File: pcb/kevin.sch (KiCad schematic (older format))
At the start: 70 parts, among them J1 battery, J2 joystick, J3 eink, J3-DRV1 eink, SW00 SW_Push, SW01 SW_Push, SW02 SW_Push, SW03 SW_Push, SW04 SW_Push, SW05 SW_Push, SW10 SW_Push, SW11 SW_Push, SW12 SW_Push, SW13 SW_Push, SW14 SW_Push, SW15 SW_Push, SW20 SW_Push, SW21 SW_Push, SW22 SW_Push, SW23 SW_Push, SW24 SW_Push, SW25 SW_Push, SW32 SW_Push, SW33 SW_Push, SW34 SW_Push, SW35 SW_Push, U1 nice_nano

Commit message: Prepare reversible matrix (kailth pg1350 and diode footprints) Routing e-ink reset to mcu Keys placement
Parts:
- D00, D01, D02, D03, D04, D05, D10, D11, D12, D13, D14, D15, D20, D21, D22, D23, D24, D25, D32, D33, D34, D35, D_EI1: footprint Diode_SMD:D_SOD-123 -> kevin:D_SOD-123_reversible
- SW00, SW01, SW02, SW03, SW04, SW05, SW10, SW11, SW12, SW13, SW14, SW15, SW20, SW21, SW22, SW23, SW24, SW25, SW32, SW33, SW34, SW35: footprint Keebio-Parts:Kailh-PG1350-1u-reversible -> kevin:Kailh-PG1350-1u-choc-reversible
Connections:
- net labels added: eink_reset
- no-connect marks 5 -> 4

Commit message: General cleaning
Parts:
- D_EI1: footprint kevin:D_SOD-123_reversible -> Diode_SMD:D_SOD-123
- U1: footprint nice-nano-kicad:nice_nano -> kevin:nice_nano_v2_reversible; symbol nice_nano:nice_nano -> kevin:nice_nano_v2
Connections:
- no-connect marks 4 -> 6
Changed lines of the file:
@@
 Text GLabel 9000 2850 0    50   Input ~ 0
 row0
-Connection ~ 9000 2250
 Wire Wire Line
 	9000 2350 9000 2250
@@
 $EndComp
 $Comp
-L nice_nano:nice_nano U1
+L kevin:nice_nano_v2 U1
 U 1 1 60FB3122
 P 9700 2600
 F 0 "U1" H 9700 3537 60  0000 C CNN
 F 1 "nice_nano" H 9700 3431 60  0000 C CNN
-F 2 "nice-nano-kicad:nice_nano" V 10750 100 60  0001 C CNN
+F 2 "kevin:nice_nano_v2_reversible" V 10750 100 60  0001 C CNN
 F 3 "" V 10750 100 60  0001 C CNN
 	1    9700 2600
@@
 F 0 "D_EI1" V 3496 5920 50  0000 R CNN
 F 1 "MBR0530" V 3405 5920 50  0000 R CNN
-F 2 "kevin:D_SOD-123_reversible" H 3450 6000 50  0001 C CNN
+F 2 "Diode_SMD:D_SOD-123" H 3450 6000 50  0001 C CNN
 F 3 "~" H 3450 6000 50  0001 C CNN
 	1    3450 6000
@@
 Text GLabel 9000 2050 0    50   Input ~ 0
 eink_reset
+NoConn ~ 10400 1950
+NoConn ~ 9000 1950
 $EndSCHEMATC

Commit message: prepare schema for review
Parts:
- added C20: 100nF, Capacitor_SMD:C_0805_2012Metric_Pad1.18x1.45mm_HandSolder, symbol Device:C_Small
- added C21: 4.7uF, Capacitor_SMD:C_0805_2012Metric_Pad1.18x1.45mm_HandSolder, symbol Device:C_Small
- added D40, D41, D42, D43, D44: D, kevin:D_SOD-123_reversible, symbol Device:D
- added J4: to-trackball-side, Connector_PinSocket_2.54mm:PinSocket_1x08_P2.54mm_Horizontal, symbol Connector_Generic:Conn_01x08
- added J5: trackball-side, Connector_PinSocket_2.54mm:PinSocket_1x08_P2.54mm_Horizontal, symbol Connector_Generic:Conn_01x08
- added R002, R01, R02: 10k, kevin:R_1206_reversible, symbol Device:R
- added R23: 10k, Resistor_SMD:R_1206_3216Metric_Pad1.30x1.75mm_HandSolder, symbol Device:R
- added SW_4dir1: SW_4dir-push, symbol kevin:SW_SKRH-4dir-push
- added U2: XC6206P202MR-G, Package_TO_SOT_SMD:SOT-23, symbol Regulator_Linear:XC6206PxxxMR
- added U3: PMW3360DM-T2QU, kevin:IC_PMW3360DM-T2QU, symbol kevin:PMW3360DM-T2QU
- C01: renamed from C1; footprint Capacitor_SMD:C_0805_2012Metric_Pad1.18x1.45mm_HandSolder -> kevin:C_0805_reversible
- C02: renamed from C2; footprint Capacitor_SMD:C_0805_2012Metric_Pad1.18x1.45mm_HandSolder -> kevin:C_0805_reversible
- C03: renamed from C3; footprint Capacitor_SMD:C_0805_2012Metric_Pad1.18x1.45mm_HandSolder -> kevin:C_0805_reversible
- C04: renamed from C4; footprint Capacitor_SMD:C_0805_2012Metric_Pad1.18x1.45mm_HandSolder -> kevin:C_0805_reversible
- C05: renamed from C5; footprint Capacitor_SMD:C_0805_2012Metric_Pad1.18x1.45mm_HandSolder -> kevin:C_0805_reversible
- C06: renamed from C6; footprint Capacitor_SMD:C_0805_2012Metric_Pad1.18x1.45mm_HandSolder -> kevin:C_0805_reversible
- C07: renamed from C7; footprint Capacitor_SMD:C_0805_2012Metric_Pad1.18x1.45mm_HandSolder -> kevin:C_0805_reversible
- C08: renamed from C8; footprint Capacitor_SMD:C_0805_2012Metric_Pad1.18x1.45mm_HandSolder -> kevin:C_0805_reversible
- C09: renamed from C9; footprint Capacitor_SMD:C_0805_2012Metric_Pad1.18x1.45mm_HandSolder -> kevin:C_0805_reversible
- C10, C11, C12, C13, C14, C15, C16, C17: footprint Capacitor_SMD:C_0805_2012Metric_Pad1.18x1.45mm_HandSolder -> kevin:C_0805_reversible
- DS01: renamed from D_EI1; value MBR0530 -> D_Sch; footprint Diode_SMD:D_SOD-123 -> kevin:D_SOD-123_reversible; symbol Device:D -> Device:D_Schottky
- J2: value joystick -> joystick_analogic
- renumbered J3 to J03, J3-DRV1 to J3
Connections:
- net GND: now also C01.1, C02.1, C05.1, C20.1, C21.1, J4.2 (Pin_2), J5.2 (Pin_2), U2.1 (GND), U3.8 (GND); no longer C01.2, C02.2, C05.2
- net batin: now also R01.2
- net col0: now also D00.1 (K), D10.1 (K), D20.1 (K), D40.1 (K); no longer SW00.1, SW10.1, SW20.1
- net col1: now also D01.1 (K), D11.1 (K), D21.1 (K), D41.1 (K); no longer SW01.1, SW11.1, SW21.1
- net col2: now also D02.1 (K), D12.1 (K), D22.1 (K), D32.1 (K), D42.1 (K); no longer SW02.1, SW12.1, SW22.1, SW32.1
- net col3: now also D03.1 (K), D13.1 (K), D23.1 (K), D33.1 (K), D43.1 (K); no longer SW03.1, SW13.1, SW23.1, SW33.1
- net col4: now also D04.1 (K), D14.1 (K), D24.1 (K), D34.1 (K), D44.1 (K); no longer SW04.1, SW14.1, SW24.1, SW34.1
- net col5: now also D05.1 (K), D15.1 (K), D25.1 (K), D35.1 (K); no longer SW05.1, SW15.1, SW25.1, SW35.1
- net eink_busy: now also U1.28 (P1.02); no longer U1.3 (RXD/P0.08)
- net eink_cs: now also R002.2, R02.2
- net joyX: now also SW_4dir1.5 (Common)
- net reset: now also R01.1
- net row0: now also SW00.2, SW01.2, SW02.2, SW03.2, SW04.2, SW05.2; no longer D00.1 (K), D01.1 (K), D02.1 (K), D03.1 (K), D04.1 (K), D05.1 (K)
- net row1: now also SW10.2, SW11.2, SW12.2, SW13.2, SW14.2, SW15.2; no longer D10.1 (K), D11.1 (K), D12.1 (K), D13.1 (K), D14.1 (K), D15.1 (K)
- net row2: now also SW20.2, SW21.2, SW22.2, SW23.2, SW24.2, SW25.2; no longer D20.1 (K), D21.1 (K), D22.1 (K), D23.1 (K), D24.1 (K), D25.1 (K)
- net row3: now also SW32.2, SW33.2, SW34.2, SW35.2; no longer D32.1 (K), D33.1 (K), D34.1 (K), D35.1 (K)
- net spi_reset: now reaches U1.27 (P1.01)
- net spi_reset: now also J03.7 (Pin_7), J3.8 (Pin_8), J4.7 (Pin_7), J5.7 (Pin_7), U3.7 (NRESET)
- net trackball_detect: now reaches U1.29 (P1.07)
- net trackball_detect: now also J4.8 (Pin_8), J5.8 (Pin_8), U3.9 (MOTION)
- net at D05.2 (A): now also SW05.1; no longer SW05.2
- net at D00.2 (A): now also SW00.1; no longer SW00.2
- net at D04.2 (A): now also SW04.1; no longer SW04.2
- net at D03.2 (A): now also SW03.1; no longer SW03.2
- net at D02.2 (A): now also SW02.1; no longer SW02.2
- net at D01.2 (A): now also SW01.1; no longer SW01.2
- net at D32.2 (A): now also SW32.1; no longer SW32.2
- net at D10.2 (A): now also SW10.1; no longer SW10.2
- net at D11.2 (A): now also SW11.1; no longer SW11.2
- net at D12.2 (A): now also SW12.1; no longer SW12.2
- net at D13.2 (A): now also SW13.1; no longer SW13.2
- net at D14.2 (A): now also SW14.1; no longer SW14.2
- net at D15.2 (A): now also SW15.1; no longer SW15.2
- net at D20.2 (A): now also SW20.1; no longer SW20.2
- net at D21.2 (A): now also SW21.1; no longer SW21.2
- net at D22.2 (A): now also SW22.1; no longer SW22.2
- net at D23.2 (A): now also SW23.1; no longer SW23.2
- net at D24.2 (A): now also SW24.1; no longer SW24.2
- net at D25.2 (A): now also SW25.1; no longer SW25.2
- net at D35.2 (A): now also SW35.1; no longer SW35.2
- net at D34.2 (A): now also SW34.1; no longer SW34.2
- net at D33.2 (A): now also SW33.1; no longer SW33.2
- net at DS01.2 (A), J3.15 (Pin_15): now also C05.2; no longer C05.1
- removed net eink_reset: J03.7 (Pin_7), J3.8 (Pin_8), U1.2 (TXD/P0.06)
- net mosi renamed spi_mosi
- net spi_mosi: now also U1.2 (TXD/P0.06), J4.3 (Pin_3), J5.3 (Pin_3), U3.11 (MOSI); no longer U1.7 (P0.20)
- net sclk renamed spi_clk
- net spi_clk: now also J4.5 (Pin_5), J5.5 (Pin_5), U3.10 (SCLK)
- net vcc_ext renamed vdd_3v3
- net vdd_3v3: now also C01.2, C02.2, J4.1 (Pin_1), J5.1 (Pin_1), R002.1, R02.1, R23.1, U2.3 (VI), U3.5 (VDDIO); no longer C01.1, C02.1
- new net: D42.2 (A), SW_4dir1.1 (A)
- new net: D41.2 (A), SW_4dir1.2 (Center)
- new net: D40.2 (A), SW_4dir1.3 (C)
- new net: D43.2 (A), SW_4dir1.4 (B)
- new net: D44.2 (A), SW_4dir1.6 (D)
- new net: C20.2, C21.2, U3.3 (VDDPIX)
- new net spi_miso: J4.4 (Pin_4), J5.4 (Pin_4), U1.3 (RXD/P0.08), U3.12 (MISO)
- new net trackball_cs: J4.6 (Pin_6), J5.6 (Pin_6), R23.2, U1.7 (P0.20), U3.13 (NCS)
- new net vdd_2v: U2.2 (VO), U3.15 (LED_P), U3.4 (VDD)
- no-connect marks 6 -> 8
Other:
- note added: "(used for PMW3360)"
- note added: "Display"
- note added: "LDO"
- note added: "MCU"
- note added: "Matrix"
- note added: "NB: joystick footprints are overlapped\n(only one physical joystick is connected:\neither analog or numeric)\njoyX and row4 share a pin on MCU"
- note added: "Pointers"
- note added: "Power & reset"
- note added: "Tmp (to be removed)"
- note added: "Trackball (linked by pogo connector)"
- note added: "connector (pogo)\nfrom main pcb -->"
- note added: "connector (pogo)\nto external trackball -->"
- note added: "e-ink\nWaveshare 1.02inch e-Paper (without built-in driver)"
- note added: "https://www.waveshare.com/w/upload/2/2b/1.02inch-e-Paper_Specification.pdf"
- note added: "lithium battery 3.7V"
- note added: "numeric joystick"
- note added: "on/off switch"
- note added: "reset button"
- note removed: "e-ink without built-in driver"
- note removed: "https://www.waveshare.com/product/displays/e-paper/epaper-3/1.02inch-e-paper-module.htm"
- note removed: "https://www.waveshare.com/product/displays/e-paper/epaper-3/1.02inch-e-paper.htm"
- note removed: "https://www.waveshare.com/wiki/1.02inch_e-Paper_Module"
- note removed: "power (lithium battery 3.7V)"
- note removed: "reset"
- moved on the sheet: BT1, C01, C02, C03, C04, C05, C06, C07, C08, C09, C10, C11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

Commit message: minor correction on schematic layout + first attempt to route traces
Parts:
- removed R01: 10k, kevin:R_1206_reversible, symbol Device:R
- DS01: symbol Device:D_Schottky -> Device:D_Schottky_Small
- J2: footprint Connector_FFC-FPC:Molex_200528-0050_1x05-1MP_P1.00mm_Horizontal -> Connector_FFC-FPC:Molex_200528-0040_1x04-1MP_P1.00mm_Horizontal
- J3: footprint Connector_FFC-FPC:Hirose_FH12-30S-0.5SH_1x30-1MP_P0.50mm_Horizontal -> kevin:Hirose_FH12-30S-0.5SH_1x30-1MP_P0.50mm_Horizontal_reversible
- SW_RST_1: footprint random-keyboard-parts:SKQG-1155865 -> kevin:SKQGADE010_reversible
- renumbered C06 to C05, C07 to C06, C08 to C07, C05 to C08, J03 to J903, R002 to R902
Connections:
- net GND: now also C08.2; no longer C08.1
- net col2: now also U1.26 (NFC1/P0.09); no longer U1.23 (P1.13)
- net col3: now also U1.25 (NFC2/P0.10); no longer U1.24 (P1.11)
- net col4: now also U1.24 (P1.11); no longer U1.25 (NFC2/P0.10)
- net col5: now also U1.23 (P1.13); no longer U1.26 (NFC1/P0.09)
- net at DS01.2 (A), J3.15 (Pin_15): now also C08.1; no longer C08.2
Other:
- moved on the sheet: C08, DS01
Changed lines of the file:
@@
 $EndDescr
 $Comp
-L Connector_Generic:Conn_01x08 J03
+L Connector_Generic:Conn_01x08 J903
 U 1 1 60FE5604
 P 13095 1410
-F 0 "J03" H 13175 1402 50  0000 L CNN
+F 0 "J903" H 13175 1402 50  0000 L CNN
 F 1 "eink" H 13175 1311 50  0000 L CNN
 F 2 "Connector_PinSocket_2.54mm:PinSocket_1x08_P2.54mm_Horizontal" H 13095 1410 50  0001 C CNN
@@
 	12220 1110 12295 1110
 $Comp
-L Device:R R002
+L Device:R R902
 U 1 1 614C56E7
 P 12295 1310
-F 0 "R002" H 12365 1356 50  0000 L CNN
+F 0 "R902" H 12365 1356 50  0000 L CNN
 F 1 "10k" H 12365 1265 50  0000 L CNN
 F 2 "kevin:R_1206_reversible" V 12225 1310 50  0001 C CNN
@@
 F 0 "J2" H 3555 4617 50  0000 L CNN
 F 1 "joystick_analogic" H 3555 4526 50  0000 L CNN
-F 2 "Connector_FFC-FPC:Molex_200528-0050_1x05-1MP_P1.00mm_Horizontal" H 3475 4625 50  0001 C CNN
+F 2 "Connector_FFC-FPC:Molex_200528-0040_1x04-1MP_P1.00mm_Horizontal" H 3475 4625 50  0001 C CNN
 F 3 "~" H 3475 4625 50  0001 C CNN
 	1    3475 4625
@@
 F 0 "J3" H 11030 2617 50  0000 L CNN
 F 1 "eink" H 11030 2526 50  0000 L CNN
-F 2 "Connector_FFC-FPC:Hirose_FH12-30S-0.5SH_1x30-1MP_P0.50mm_Horizontal" H 10950 2625 50  0001 C CNN
+F 2 "kevin:Hirose_FH12-30S-0.5SH_1x30-1MP_P0.50mm_Horizontal_reversible" H 10950 2625 50  0001 C CNN
 F 3 "~" H 10950 2625 50  0001 C CNN
 	1    10950 2625
@@
 $EndComp
 $Comp
-L Device:D_Schottky DS01
+L Device:D_Schottky_Small DS01
 U 1 1 614E26FF
-P 9475 2625
-F 0 "DS01" V 9521 2545 50  0000 R CNN
-F 1 "D_Sch" V 9430 2545 50  0000 R CNN
-F 2 "kevin:D_SOD-123_reversible" H 9475 2625 50  0001 C CNN
-F 3 "~" H 9475 2625 50  0001 C CNN
-	1    9475 2625
+P 9425 2625
+F 0 "DS01" V 9471 2545 50  0000 R CNN
+F 1 "D_Sch" V 9380 2545 50  0000 R CNN
+F 2 "kevin:D_SOD-123_reversible" H 9425 2625 50  0001 C CNN
+F 3 "~" H 9425 2625 50  0001 C CNN
+	1    9425 2625
 	1    0    0    -1
 $EndComp
@@
 $EndComp
 $Comp
-L Device:C_Small C07
+L Device:C_Small C06
 U 1 1 61669C1A
 P 10375 2425
-F 0 "C07" V 10146 2425 50  0000 C CNN
+F 0 "C06" V 10146 2425 50  0000 C CNN
 F 1 "1uF" V 10237 2425 50  0000 C CNN
 F 2 "kevin:C_0805_reversible" H 10375 2425 50  0001 C CNN
@@
 $EndComp
 $Comp
-L Device:C_Small C06
+L Device:C_Small C05
 U 1 1 61669F0B
 P 10650 2325
-F 0 "C06" V 10421 2325 50  0000 C CNN
+F 0 "C05" V 10421 2325 50  0000 C CNN
 F 1 "1uF" V 10512 2325 50  0000 C CNN
 F 2 "kevin:C_0805_reversible" H 10650 2325 50  0001 C CNN
@@
 $EndComp
 $Comp
-L Device:C_Small C08
+L Device:C_Small C07
 U 1 1 616697D2
 P 10650 2525
-F 0 "C08" V 10421 2525 50  0000 C CNN
+F 0 "C07" V 10421 2525 50  0000 C CNN
 F 1 "1uF" V 10512 2525 50  0000 C CNN
 F 2 "kevin:C_0805_reversible" H 10650 2525 50  0001 C CNN
@@
 Text Notes 8800 4975 0    50   ~ 0
 lithium battery 3.7V
-$Comp
-L Device:R R01
-U 1 1 6111EB34
-P 7925 5525
-F 0 "R01" H 7995 5571 50  0000 L CNN
-F 1 "10k" H 7995 5480 50  0000 L CNN
-F 2 "kevin:R_1206_reversible" V 7855 5525 50  0001 C CNN
-F 3 "~" H 7925 5525 50  0001 C CNN
-	1    7925 5525
-	1    0    0    -1
-$EndComp
-Text GLabel 7925 5675 3    50   Input ~ 0
-batin
 Connection ~ 6600 1675
 Text GLabel 7300 3075 3    50   Input ~ 0
@@
 Text GLabel 8000 1475 2    50   Input ~ 0
 batin
-Text GLabel 8000 2575 2    50   Input ~ 0
-col5
-Text GLabel 8000 2475 2    50   Input ~ 0
-col4
-Text GLabel 8000 2375 2    50   Input ~ 0
-col3
-Text GLabel 8000 2275 2    50   Input ~ 0
-col2
-Text GLabel 8000 2175 2    50   Input ~ 0
-col1
-Text GLabel 8000 2075 2    50   Input ~ 0
-col0
 $Comp
 L power:GND #PWR0105
@@
 F 0 "SW_RST_1" H 8125 5660 50  0000 C CNN
 F 1 "SW_Push" H 8125 5569 50  0000 C CNN
-F 2 "random-keyboard-parts:SKQG-1155865" H 8125 5575 50  0001 C CNN
+F 2 "kevin:SKQGADE010_reversible" H 8125 5575 50  0001 C CNN
 F 3 "~" H 8125 5575 50  0001 C CNN
 	1    8125 5375
@@
 Connection ~ 3600 6875
 $Comp
-L Device:C_Small C05
+L Device:C_Small C08
 U 1 1 614E2176
-P 9425 3050
-F 0 "C05" V 9196 3050 50  0000 C CNN
-F 1 "1uF" V 9287 3050 50  0000 C CNN
-F 2 "kevin:C_0805_reversible" H 9425 3050 50  0001 C CNN
-F 3 "~" H 9425 3050 50  0001 C CNN
-	1    9425 3050
-	0    -1   -1   0
+P 9425 3225
+F 0 "C08" V 9196 3225 50  0000 C CNN
+F 1 "1uF" V 9287 3225 50  0000 C CNN
+F 2 "kevin:C_0805_reversible" H 9425 3225 50  0001 C CNN
+F 3 "~" H 9425 3225 50  0001 C CNN
+	1    9425 3225
+	0    1    1    0
 $EndComp
 Wire Wire Line
@@
 Text Notes 9850 2100 0    39   Italic 0
 4-line SPI
-Text GLabel 7850 5375 0    50   Output ~ 0
+Text GLabel 7925 5375 0    50   Output ~ 0
 reset
-Wire Wire Line
-	7850 5375 7925 5375
-Connection ~ 7925 5375
 $Comp
 L Device:R R02
@@
 	9525 2225 10750 2225
 Connection ~ 9525 2225
-Wire Wire Line
-	9625 2625 10750 2625
-Wire Wire Line
-	9325 2425 9325 2625
-Wire Wire Line
-	9325 2625 9325 3050
-Connection ~ 9325 2625
 $Comp
 L Device:C_Small C09
@@
 	0    1    1    0
 $EndComp
-Wire Wire Line
-	9525 3050 9625 3050
-Wire Wire Line
-	9625 3050 9625 2625
-Connection ~ 9625 2625
 Connection ~ 5225 6975
 Wire Wire Line
@@
 Wire Wire Line
 	9375 1225 9700 1225
+Wire Wire Line
+	9325 2425 9325 2625
+Connection ~ 9325 2625
+Wire Wire Line
+	9325 2625 9325 3225
+Wire Wire Line
+	9525 2625 9525 3225
+Wire Wire Line
+	9525 2625 10750 2625
+Connection ~ 9525 2625
+Text GLabel 8000 2075 2    50   Input ~ 0
+col0
+Text GLabel 8000 2175 2    50   Input ~ 0
+col1
+Text GLabel 8000 2575 2    50   Input ~ 0
+col2
+Text GLabel 8000 2475 2    50   Input ~ 0
+col3
+Text GLabel 8000 2375 2    50   Input ~ 0
+col4
+Text GLabel 8000 2275 2    50   Input ~ 0
+col5
 $EndSCHEMATC

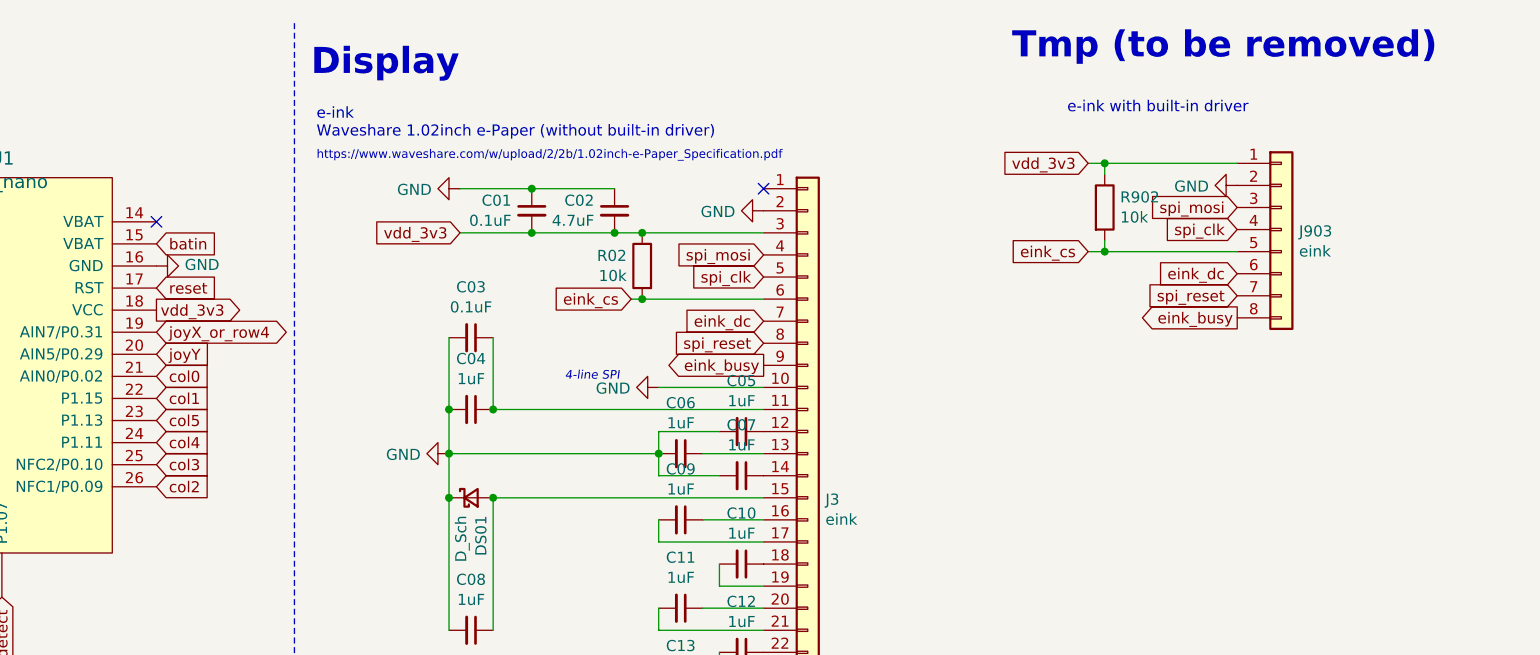
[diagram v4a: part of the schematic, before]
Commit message: footprints work auto-routing traces
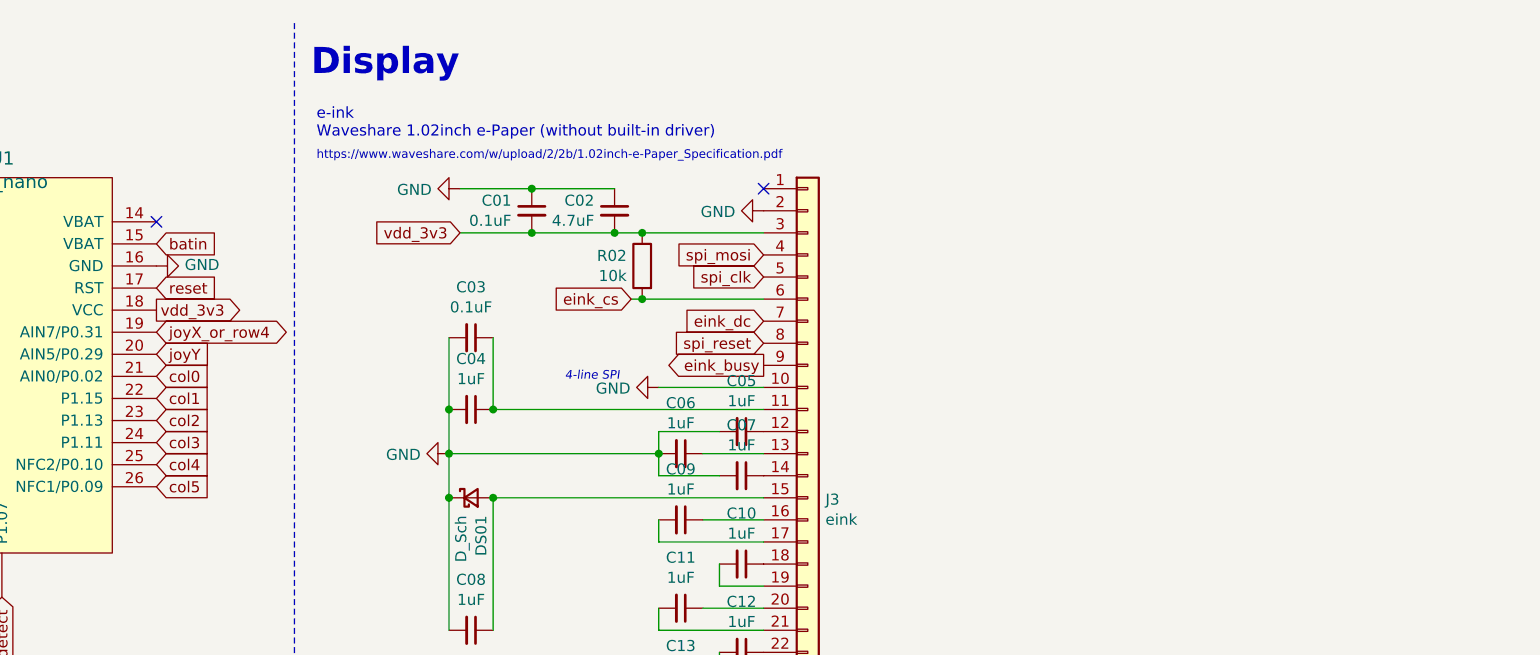
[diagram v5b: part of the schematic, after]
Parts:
- removed J903: eink, Connector_PinSocket_2.54mm:PinSocket_1x08_P2.54mm_Horizontal, symbol Connector_Generic:Conn_01x08
- removed R902: 10k, kevin:R_1206_reversible, symbol Device:R
- SW_4dir1: footprint (none) -> kevin:Alpsalpine skrhade010
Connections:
- net col2: now also U1.23 (P1.13); no longer U1.26 (NFC1/P0.09)
- net col3: now also U1.24 (P1.11); no longer U1.25 (NFC2/P0.10)
- net col4: now also U1.25 (NFC2/P0.10); no longer U1.24 (P1.11)
- net col5: now also U1.26 (NFC1/P0.09); no longer U1.23 (P1.13)
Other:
- note removed: "Tmp (to be removed)"
- note removed: "e-ink with built-in driver"
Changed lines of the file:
@@
 Comment4 "Half part of split keyboard"
 $EndDescr
-$Comp
-L Connector_Generic:Conn_01x08 J903
-U 1 1 60FE5604
-P 13095 1410
-F 0 "J903" H 13175 1402 50  0000 L CNN
-F 1 "eink" H 13175 1311 50  0000 L CNN
-F 2 "Connector_PinSocket_2.54mm:PinSocket_1x08_P2.54mm_Horizontal" H 13095 1410 50  0001 C CNN
-F 3 "~" H 13095 1410 50  0001 C CNN
-	1    13095 1410
-	1    0    0    -1
-$EndComp
-Text GLabel 12895 1310 0    50   Input ~ 0
-spi_mosi
-Text GLabel 12895 1410 0    50   Input ~ 0
-spi_clk
-Text GLabel 12895 1610 0    50   Input ~ 0
-eink_dc
-Text GLabel 12895 1810 0    50   Output ~ 0
-eink_busy
-Text GLabel 12220 1110 0    50   Input ~ 0
-vdd_3v3
-Text Notes 12125 890  0    50   ~ 0
-e-ink with built-in driver
-Text GLabel 12220 1510 0    50   Input ~ 0
-eink_cs
-Text GLabel 12895 1710 0    50   Input ~ 0
-spi_reset
-$Comp
-L power:GND #PWR0103
-U 1 1 60FE810D
-P 12895 1210
-F 0 "#PWR0103" H 12895 960 50  0001 C CNN
-F 1 "GND" V 12900 1082 50  0000 R CNN
-F 2 "" H 12895 1210 50  0001 C CNN
-F 3 "" H 12895 1210 50  0001 C CNN
-	1    12895 1210
-	0    1    1    0
-$EndComp
-Wire Wire Line
-	12220 1110 12295 1110
-$Comp
-L Device:R R902
-U 1 1 614C56E7
-P 12295 1310
-F 0 "R902" H 12365 1356 50  0000 L CNN
-F 1 "10k" H 12365 1265 50  0000 L CNN
-F 2 "kevin:R_1206_reversible" V 12225 1310 50  0001 C CNN
-F 3 "~" H 12295 1310 50  0001 C CNN
-	1    12295 1310
-	1    0    0    -1
-$EndComp
-Wire Wire Line
-	12220 1510 12295 1510
-Wire Wire Line
-	12295 1460 12295 1510
-Connection ~ 12295 1510
-Wire Wire Line
-	12295 1510 12895 1510
-Wire Wire Line
-	12295 1160 12295 1110
-Connection ~ 12295 1110
-Wire Wire Line
-	12295 1110 12895 1110
 Text GLabel 4950 5225 0    50   Output ~ 0
 trackball_detect
@@
 F 0 "SW_4dir1" H 1725 5475 50  0000 C CNN
 F 1 "SW_4dir-push" H 1725 5384 50  0000 C CNN
-F 2 "" H 1625 5700 50  0001 C CNN
+F 2 "kevin:Alpsalpine skrhade010" H 1625 5700 50  0001 C CNN
 F 3 "https://tech.alpsalpine.com/prod/e/html/multicontrol/switch/skrh/skrhade010.html" H 1625 5700 50  0001 C CNN
 	1    1725 5100
@@
 	1    0    0    -1
 $EndComp
-Text Notes 11875 650  0    118  ~ 24
-Tmp (to be removed)
 Wire Notes Line width 8 style solid
 	8625 475  8625 4250
@@
 Text GLabel 8000 2175 2    50   Input ~ 0
 col1
+Text GLabel 8000 2275 2    50   Input ~ 0
+col2
+Text GLabel 8000 2375 2    50   Input ~ 0
+col3
+Text GLabel 8000 2475 2    50   Input ~ 0
+col4
 Text GLabel 8000 2575 2    50   Input ~ 0
-col2
-Text GLabel 8000 2475 2    50   Input ~ 0
-col3
-Text GLabel 8000 2375 2    50   Input ~ 0
-col4
-Text GLabel 8000 2275 2    50   Input ~ 0
 col5
 $EndSCHEMATC
